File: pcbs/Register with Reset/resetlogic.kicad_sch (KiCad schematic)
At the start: 12 parts, among them U401 74HC08, U402 74HC14

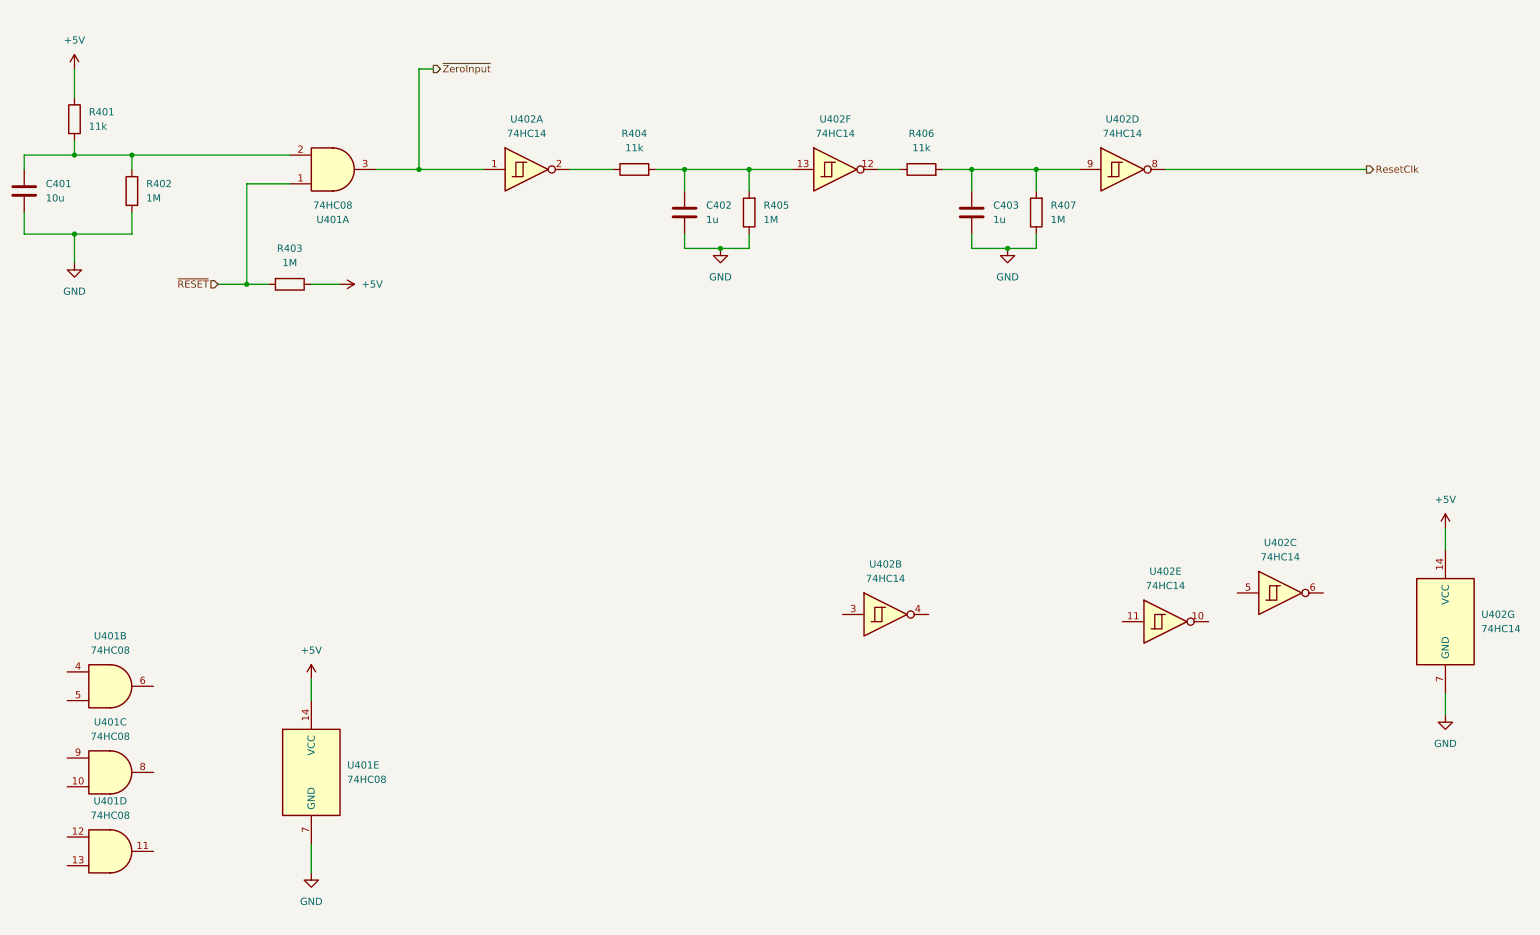
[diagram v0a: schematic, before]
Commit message: First draft of whole board
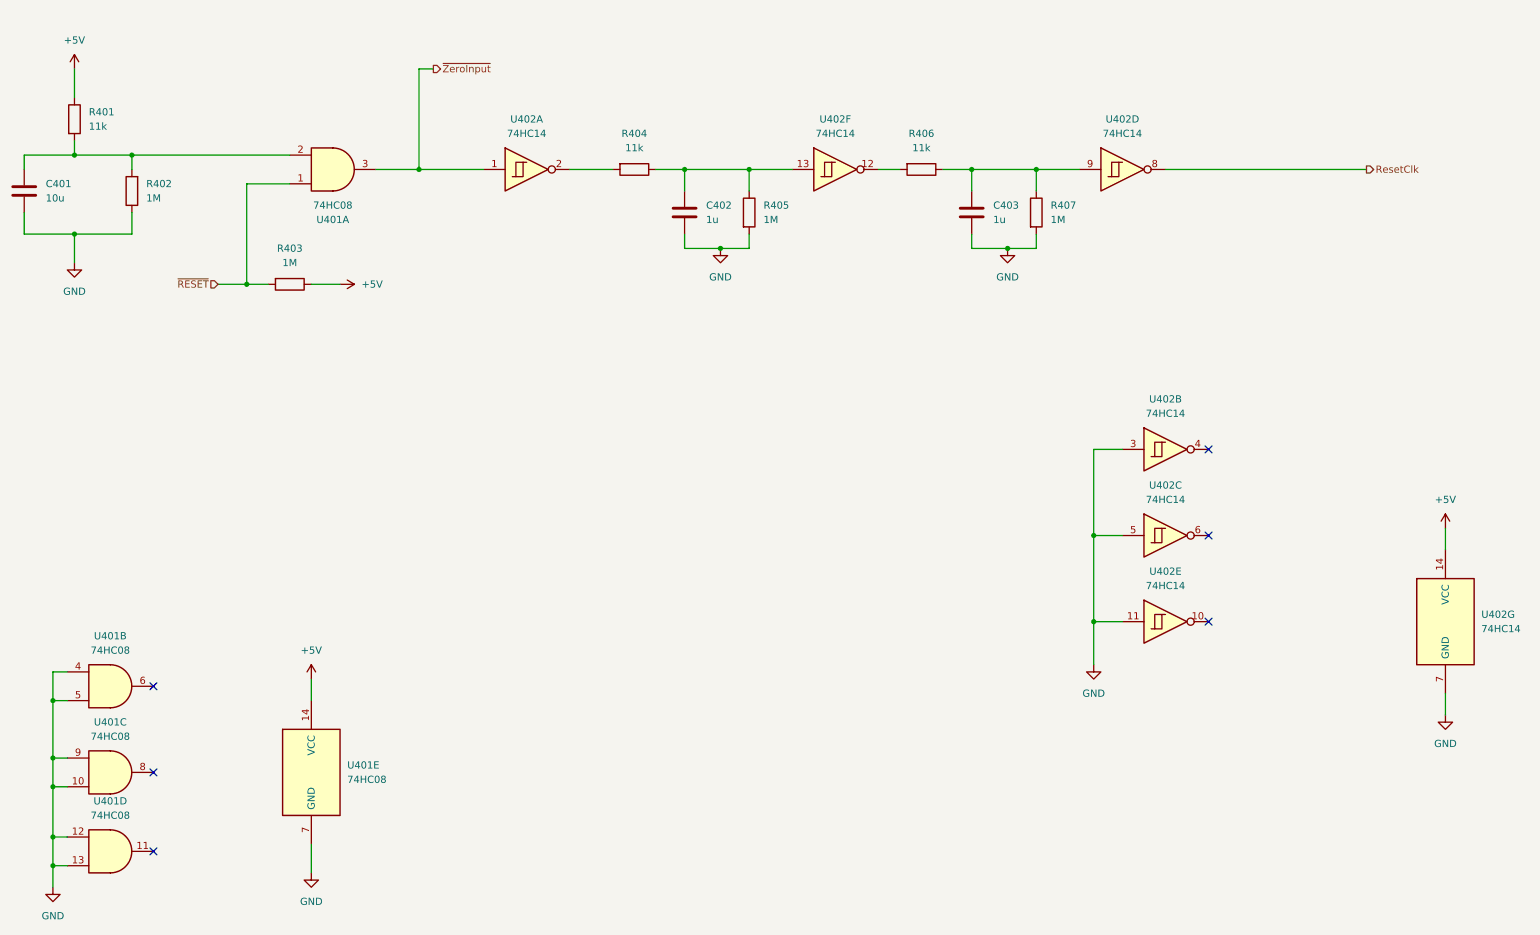
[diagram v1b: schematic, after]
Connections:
- net GND: now also R405.2, R407.2, U401.10, U401.12, U401.13, U401.4, U401.5, U401.9, U402.11, U402.3, U402.5; no longer R405.1, R407.1
- net at U402.2: now also R404.2; no longer R404.1
- net at U402.12: now also R406.2; no longer R406.1
- net at C402.1, U402.13: now also R404.1, R405.1; no longer R404.2, R405.2
- net at C403.1, U402.9: now also R406.1, R407.1; no longer R406.2, R407.2
- no-connect marks 0 -> 6
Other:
- moved on the sheet: R404, R405, R406, R407, U402B, U402C

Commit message: Fix the reset logic....
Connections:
- net GND: no longer U402.3
- net ZeroInput: now reaches U402.4
- net ~{ZeroInput}: no longer names the net of U401.3, U402.1
- net ~{ZeroInput}: now also U402.3
- no-connect marks 6 -> 5
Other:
- moved on the sheet: U402B
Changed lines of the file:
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@@
-	)
-	(junction
-		(at 205.74 120.65)
-		(diameter 0)
-		(color 0 0 0 0)
 	)
 	(junction
@@
 		(at 39.37 162.56)
 	)
-	(no_connect
-		(at 226.06 105.41)
-	)
 	(wire
 		(pts
@@
 	(wire
 		(pts
-			(xy 205.74 120.65) (xy 205.74 105.41)
-		)
-		(stroke
-			(width 0)
-			(type default)
-		)
-	)
-	(wire
-		(pts
 			(xy 25.4 53.34) (xy 35.56 53.34)
 		)
@@
 	(wire
 		(pts
+			(xy 104.14 38.1) (xy 111.76 38.1)
+		)
+		(stroke
+			(width 0)
+			(type default)
+		)
+	)
+	(wire
+		(pts
 			(xy 144.78 55.88) (xy 152.4 55.88)
 		)
@@
 		(pts
 			(xy 21.59 144.78) (xy 24.13 144.78)
-		)
-		(stroke
-			(width 0)
-			(type default)
-		)
-	)
-	(wire
-		(pts
-			(xy 205.74 105.41) (xy 210.82 105.41)
 		)
 		(stroke
@@
 		)
 	)
-	(hierarchical_label "~{ZeroInput}"
+	(hierarchical_label "ZeroInput"
 		(shape output)
-		(at 88.9 38.1 0)
+		(at 111.76 38.1 0)
 		(fields_autoplaced yes)
 		(effects
@@
 	(symbol
 		(lib_id "74xx:74HC14")
-		(at 218.44 105.41 0)
+		(at 96.52 38.1 0)
 		(unit 2)
 		(exclude_from_sim no)
@@
 		(fields_autoplaced yes)
 		(property "Reference" "U402"
-			(at 218.44 96.52 0)
+			(at 96.52 29.21 0)
 			(effects
 				(font
@@
 		)
 		(property "Value" "74HC14"
-			(at 218.44 99.06 0)
+			(at 96.52 31.75 0)
 			(effects
 				(font
@@
 		)
 		(property "Footprint" "Package_SO:SOIC-14_3.9x8.7mm_P1.27mm"
-			(at 218.44 105.41 0)
+			(at 96.52 38.1 0)
 			(effects
 				(font
@@
 		)
 		(property "Datasheet" "https://wmsc.lcsc.com/wmsc/upload/file/pdf/v2/lcsc/1811141851_Nexperia-74HC14D-653_C5605.pdf"
-			(at 218.44 105.41 0)
+			(at 96.52 38.1 0)
 			(effects
 				(font
@@
 		)
 		(property "Description" "Hex inverter schmitt trigger"
-			(at 218.44 105.41 0)
+			(at 96.52 38.1 0)
 			(effects
 				(font
@@
 		)
 		(property "LCSC" "C5605"
-			(at 218.44 105.41 0)
-			(effects
-				(font
+			(at 96.52 38.1 0)
+			(effects
+				(font

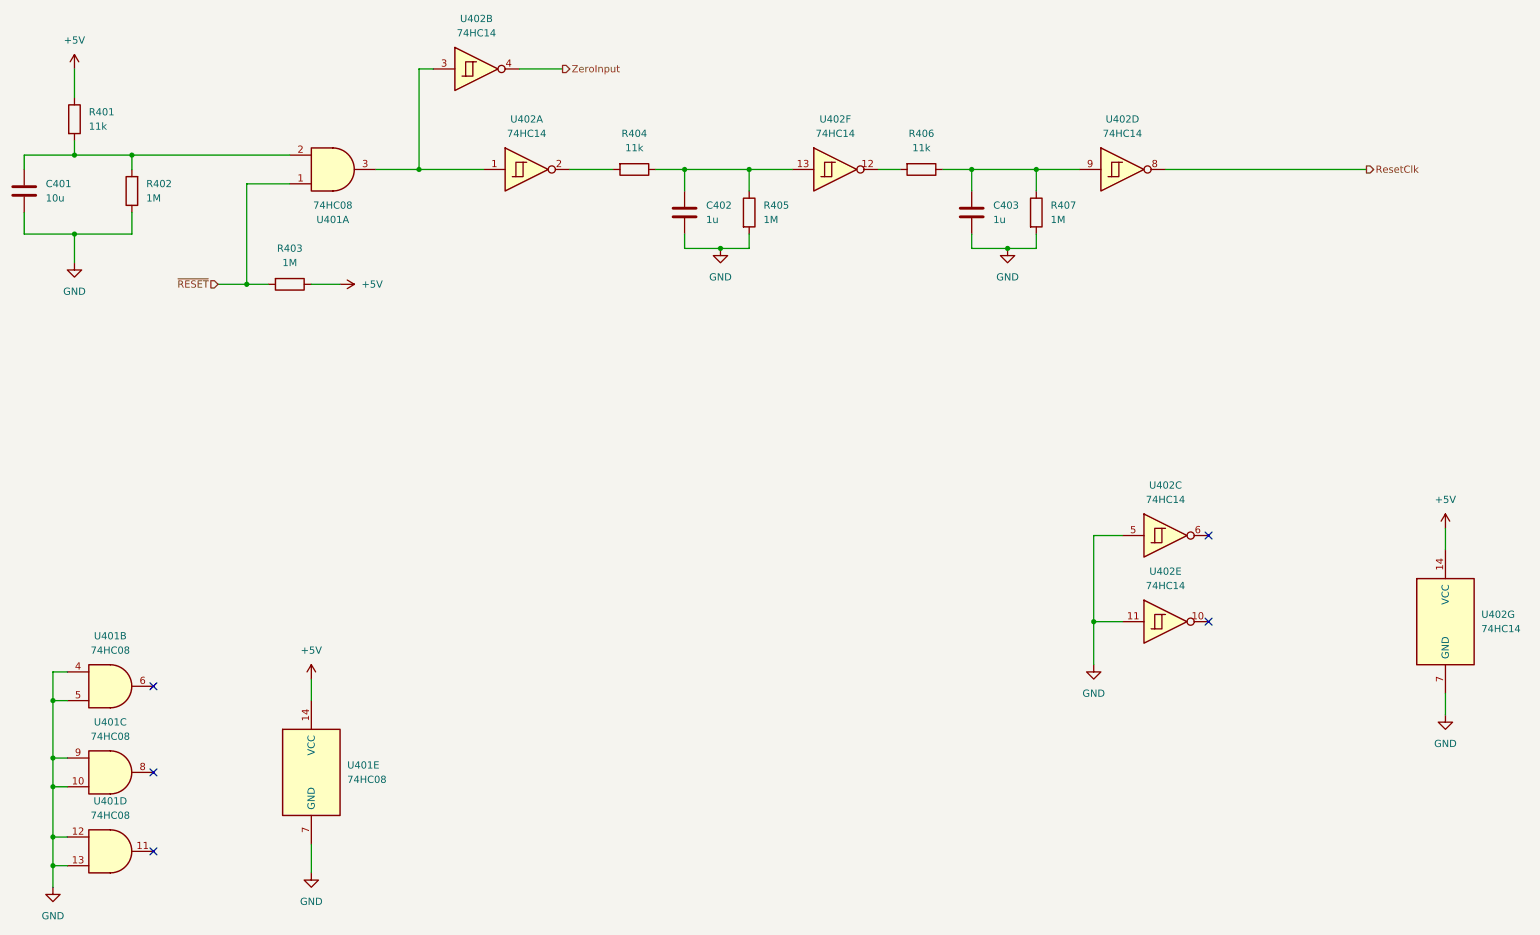
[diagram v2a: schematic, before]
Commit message: Revise the Register with Reset (#3)
Updates to Register-with-Reset:

- Convert to edge connector
- Route clock through an 'AND' with the Reset line, so the clock doesn't block reset
- Shrink the board somewhat by repositioning components
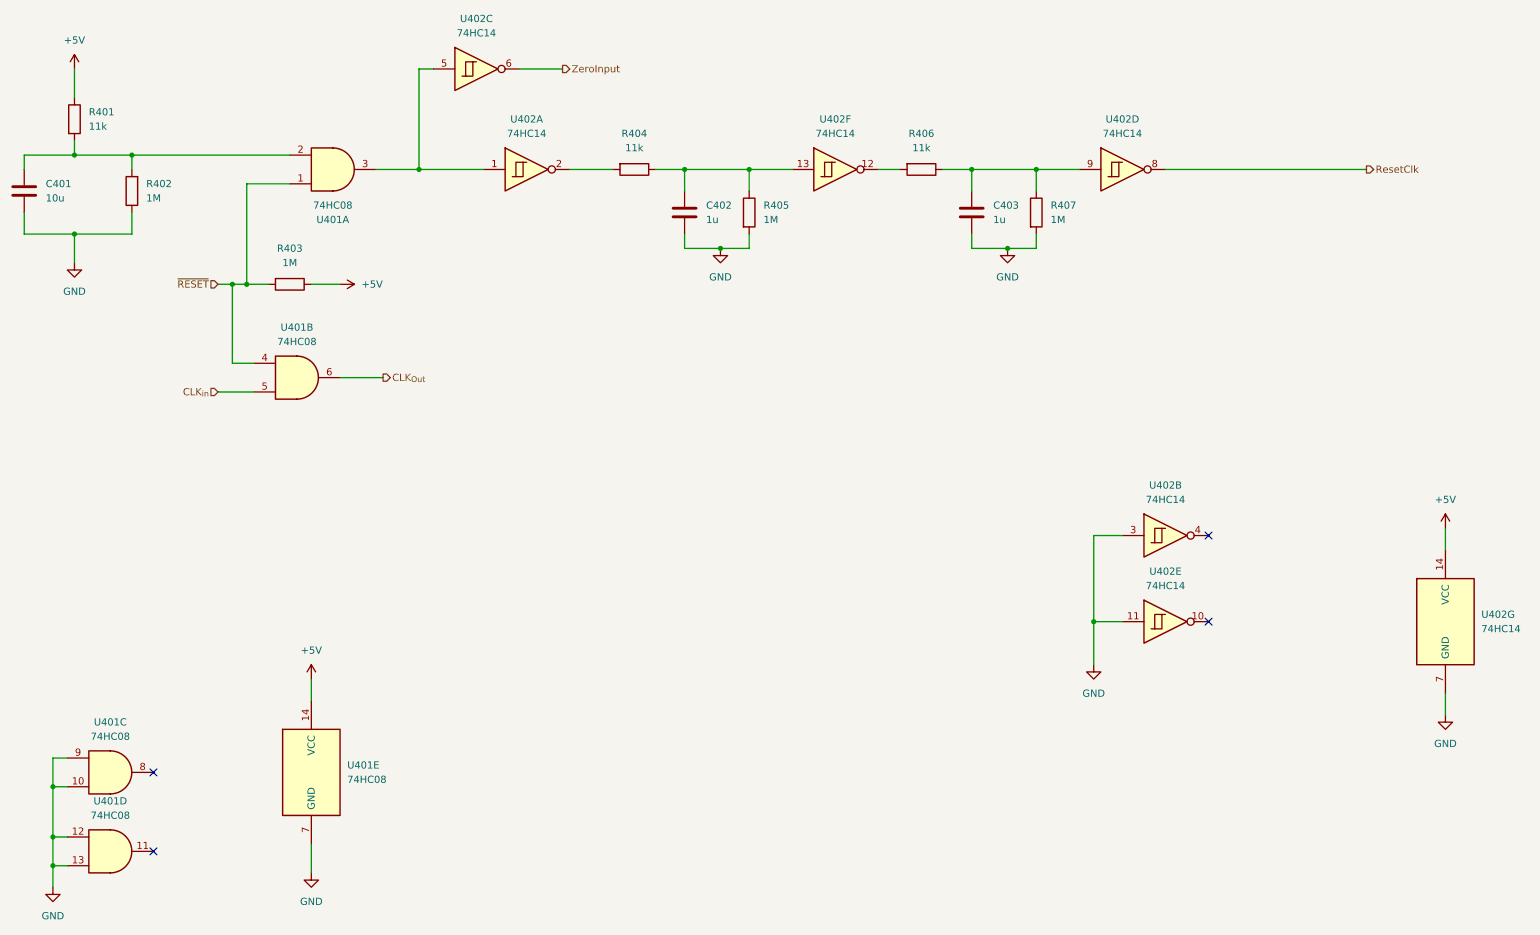
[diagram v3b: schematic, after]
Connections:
- net GND: now also U402.3; no longer U401.4, U401.5, U402.5
- net ZeroInput: now also U402.6; no longer U402.4
- net ~{RESET}: now also U401.4
- net at U401.3, U402.1: now also U402.5; no longer U402.3
- net CLK_{Out}: now reaches U401.6
- new net CLK_{in}: U401.5
- no-connect marks 5 -> 4
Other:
- moved on the sheet: U401B, U402B, U402C
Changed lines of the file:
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@@
-	)
-	(junction
-		(at 21.59 160.02)
-		(diameter 0)
-		(color 0 0 0 0)
 	)
 	(junction
@@
 	)
 	(junction
-		(at 21.59 149.86)
-		(diameter 0)
-		(color 0 0 0 0)
-	)
-	(junction
 		(at 139.7 69.85)
 		(diameter 0)
@@
 		(color 0 0 0 0)
 	)
+	(junction
+		(at 53.34 76.2)
+		(diameter 0)
+		(color 0 0 0 0)
+	)
 	(no_connect
 		(at 226.06 120.65)
@@
 	)
 	(no_connect
-		(at 39.37 147.32)
-	)
-	(no_connect
 		(at 39.37 176.53)
 	)
@@
 	(wire
 		(pts
-			(xy 21.59 160.02) (xy 21.59 149.86)
-		)
-		(stroke
-			(width 0)
-			(type default)
-		)
-	)
-	(wire
-		(pts
 			(xy 25.4 67.31) (xy 25.4 72.39)
 		)
@@
 	(wire
 		(pts
-			(xy 21.59 149.86) (xy 24.13 149.86)
-		)
-		(stroke
-			(width 0)
-			(type default)
-		)
-	)
-	(wire
-		(pts
 			(xy 67.31 76.2) (xy 72.39 76.2)
 		)
@@
 	(wire
 		(pts
+			(xy 53.34 76.2) (xy 55.88 76.2)
+		)
+		(stroke
+			(width 0)
+			(type default)
+		)
+	)
+	(wire
+		(pts
 			(xy 144.78 55.88) (xy 152.4 55.88)
 		)
@@
 	(wire
 		(pts
-			(xy 21.59 144.78) (xy 24.13 144.78)
+			(xy 53.34 90.17) (xy 57.15 90.17)
 		)
 		(stroke
@@
 	(wire
 		(pts
+			(xy 50.8 95.25) (xy 57.15 95.25)
+		)
+		(stroke
+			(width 0)
+			(type default)
+		)
+	)
+	(wire
+		(pts
 			(xy 195.58 67.31) (xy 195.58 69.85)
 		)
@@
 	(wire
 		(pts
+			(xy 72.39 92.71) (xy 80.01 92.71)
+		)
+		(stroke
+			(width 0)
+			(type default)
+		)
+	)
+	(wire
+		(pts
 			(xy 267.97 148.59) (xy 267.97 152.4)
 		)
@@
 	(wire
 		(pts
+			(xy 53.34 76.2) (xy 53.34 90.17)
+		)
+		(stroke
+			(width 0)
+			(type default)
+		)
+	)
+	(wire
+		(pts
 			(xy 21.59 165.1) (xy 21.59 160.02)
 		)
@@
 	(wire
 		(pts
-			(xy 50.8 76.2) (xy 55.88 76.2)
+			(xy 50.8 76.2) (xy 53.34 76.2)
 		)
 		(stroke
@@
 		(pts
 			(xy 25.4 50.8) (xy 25.4 53.34)
-		)
-		(stroke
-			(width 0)
-			(type default)
-		)
-	)
-	(wire
-		(pts
-			(xy 21.59 149.86) (xy 21.59 144.78)
 		)
 		(stroke
@@
 		(shape output)
 		(at 254 55.88 0)
+		(fields_autoplaced yes)
+		(effects
+			(font
+				(size 1.27 1.27)
+			)
+			(justify left)
+		)
+	)
+	(hierarchical_label "CLK_{in}"
+		(shape input)
+		(at 50.8 95.25 180)
+		(fields_autoplaced yes)
+		(effects
+			(font
+				(size 1.27 1.27)
+			)
+			(justify right)
+		)
+	)
+	(hierarchical_label "CLK_{Out}"
+		(shape output)
+		(at 80.01 92.71 0)
 		(fields_autoplaced yes)
 		(effects
@@
 	(symbol
 		(lib_id "74xx:74HC14")
-		(at 218.44 120.65 0)
+		(at 96.52 38.1 0)
 		(unit 3)
 		(exclude_from_sim no)
@@
 		(fields_autoplaced yes)
 		(property "Reference" "U402"
-			(at 218.44 111.76 0)
+			(at 96.52 29.21 0)
 			(effects
 				(font
@@
 		)
 		(property "Value" "74HC14"
-			(at 218.44 114.3 0)
+			(at 96.52 31.75 0)
 			(effects
 				(font
@@
 		)
 		(property "Footprint" "Package_SO:SOIC-14_3.9x8.7mm_P1.27mm"
-			(at 218.44 120.65 0)
+			(at 96.52 38.1 0)
 			(effects
 				(font
@@
 		)
 		(property "Datasheet" "https://wmsc.lcsc.com/wmsc/upload/file/pdf/v2/lcsc/1811141851_Nexperia-74HC14D-653_C5605.pdf"
-			(at 218.44 120.65 0)
+			(at 96.52 38.1 0)
 			(effects
 				(font
@@
 		)
 		(property "Description" "Hex inverter schmitt trigger"
-			(at 218.44 120.65 0)
+			(at 96.52 38.1 0)
 			(effects
 				(font
@@
 		)
 		(property "LCSC" "C5605"
-			(at 218.44 120.65 0)
+			(at 96.52 38.1 0)
 			(effects
 				(font
@@
 	(symbol
 		(lib_id "74xx:74LS08")
-		(at 31.75 147.32 0)
+		(at 64.77 92.71 0)
 		(unit 2)
 		(exclude_from_sim no)
@@
 		(fields_autoplaced yes)
 		(property "Reference" "U401"
-			(at 31.7417 138.43 0)
+			(at 64.7617 83.82 0)
 			(effects
 				(font
@@
 		)
 		(property "Value" "74HC08"
-			(at 31.7417 140.97 0)
+			(at 64.7617 86.36 0)
 			(effects
 				(font
@@
 		)
 		(property "Footprint" "Package_SO:SOIC-14_3.9x8.7mm_P1.27mm"
-			(at 31.75 147.32 0)
+			(at 64.77 92.71 0)
 			(effects
 				(font
@@
 		)
 		(property "Datasheet" "https://wmsc.lcsc.com/wmsc/upload/file/pdf/v2/lcsc/2304140030_Nexperia-74HC08D-653_C5593.pdf"
-			(at 31.75 147.32 0)
+			(at 64.77 92.71 0)
 			(effects
 				(font
@@
 		)
 		(property "Description" "Quad And2"
-			(at 31.75 147.32 0)
+			(at 64.77 92.71 0)
 			(effects
 				(font
@@
 		)
 		(property "LCSC" "C5593"
-			(at 31.75 147.32 0)
+			(at 64.77 92.71 0)
 			(effects
 				(font
@@
 	(symbol
 		(lib_id "74xx:74HC14")
-		(at 96.52 38.1 0)
+		(at 218.44 120.65 0)
 		(unit 2)
 		(exclude_from_sim no)
@@
 		(fields_autoplaced yes)
 		(property "Reference" "U402"
-			(at 96.52 29.21 0)
+			(at 218.44 111.76 0)
 			(effects
 				(font
@@
 		)
 		(property "Value" "74HC14"
-			(at 96.52 31.75 0)
+			(at 218.44 114.3 0)
 			(effects
 				(font
@@
 		)
 		(property "Footprint" "Package_SO:SOIC-14_3.9x8.7mm_P1.27mm"
-			(at 96.52 38.1 0)
+			(at 218.44 120.65 0)
 			(effects
 				(font
@@
 		)
 		(property "Datasheet" "https://wmsc.lcsc.com/wmsc/upload/file/pdf/v2/lcsc/1811141851_Nexperia-74HC14D-653_C5605.pdf"
-			(at 96.52 38.1 0)
+			(at 218.44 120.65 0)
 			(effects
 				(font
@@
 		)
 		(property "Description" "Hex inverter schmitt trigger"
-			(at 96.52 38.1 0)
+			(at 218.44 120.65 0)
 			(effects
 				(font
@@
 		)
 		(property "LCSC" "C5605"
-			(at 96.52 38.1 0)
-			(effects
-				(font
+			(at 218.44 120.65 0)
+			(effects
+				(font
